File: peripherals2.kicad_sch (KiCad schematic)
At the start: 10 parts, among them J4 MSD-4-A, U8 GSDA213, U9 VEML3235SL

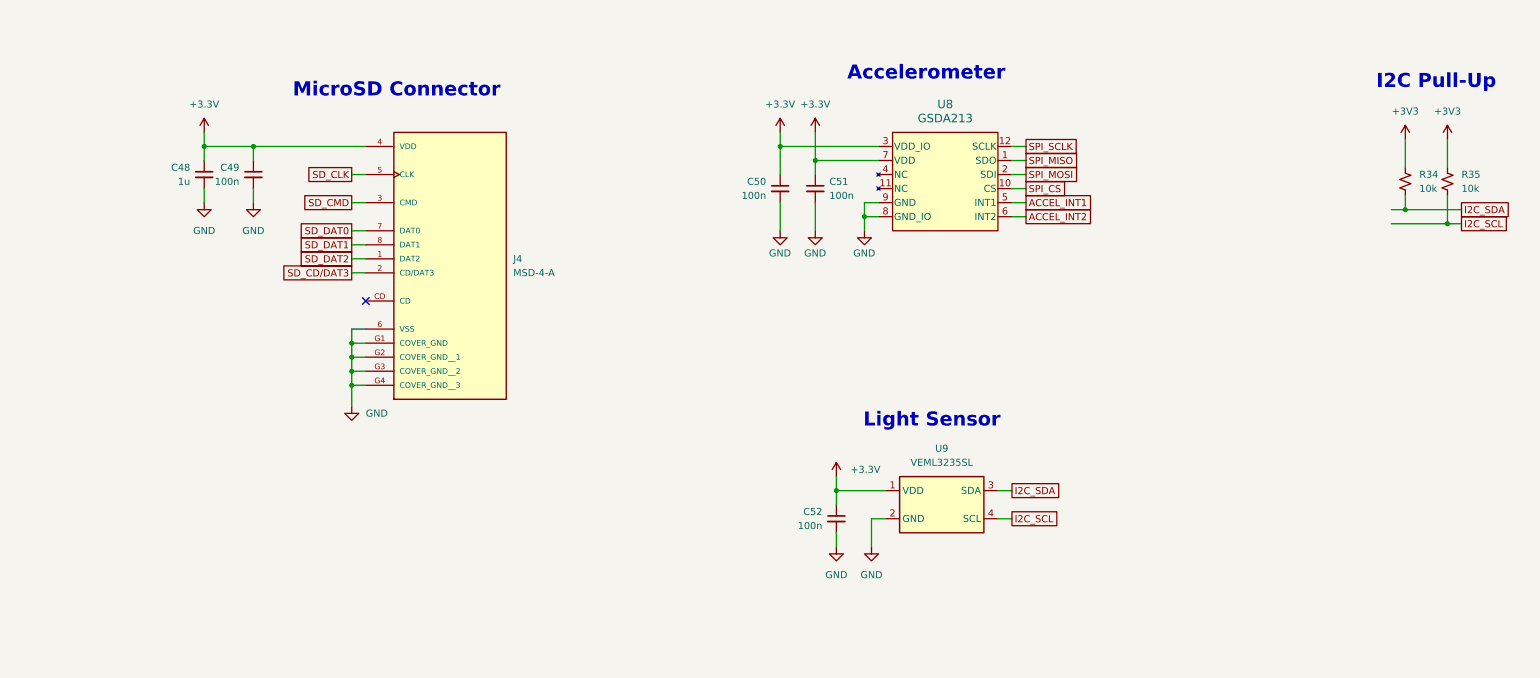
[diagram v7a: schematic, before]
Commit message: chore: adds titles to sheets and organizes root
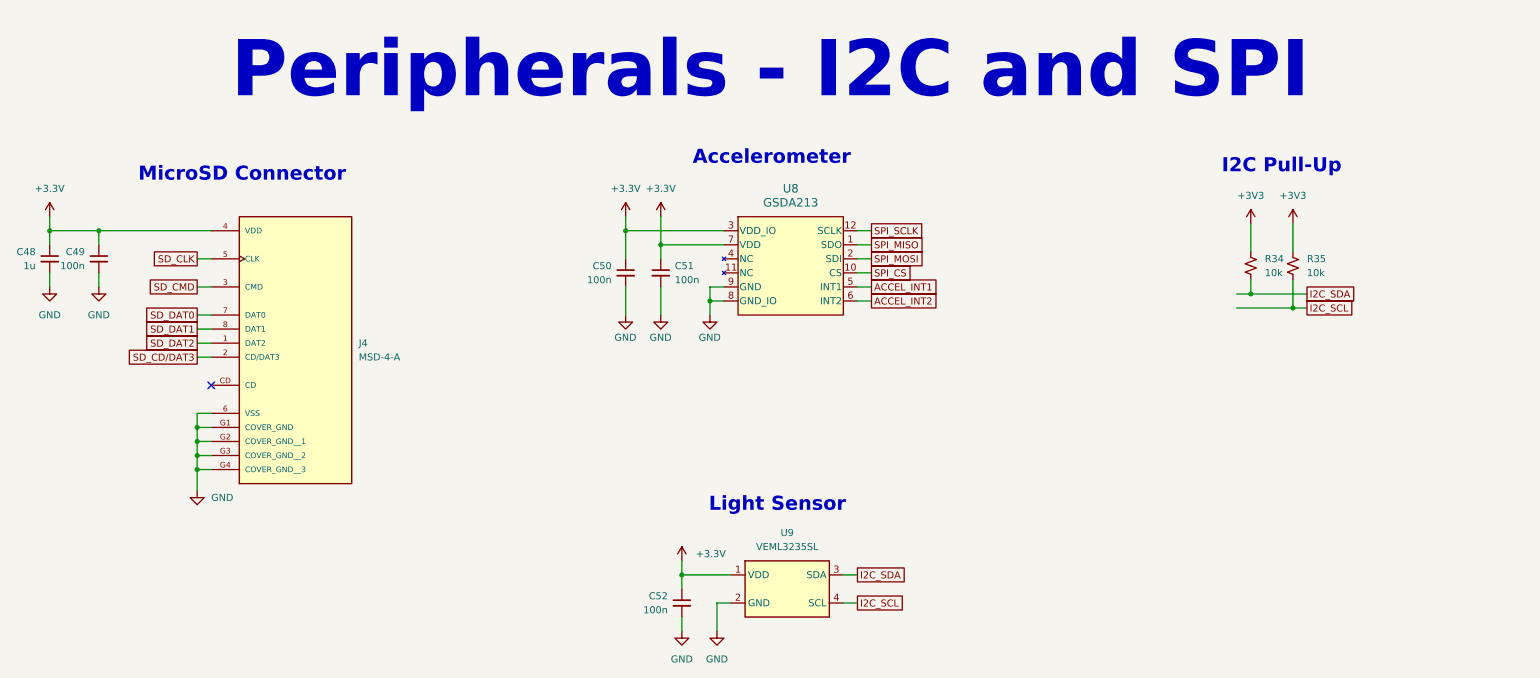
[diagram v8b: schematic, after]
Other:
- note added: "Peripherals - I2C and SPI"
- company: (none) -> Os Circuitados
- title: (none) -> Peripherals - I2C and SPI
- moved on the sheet: C48, C49, C50, C51, C52, J4, R34, R35, U8, U9
